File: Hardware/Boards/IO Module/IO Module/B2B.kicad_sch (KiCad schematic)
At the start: 0 parts

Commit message: Updated IO Module Schematics
Added Power, USB hub and USB-JTAG circuits
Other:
- company: (none) -> Drexel University
- title: (none) -> Board to Board Connectors
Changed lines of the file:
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@@
 	(generator "eeschema")
 	(generator_version "8.0")
-	(paper "A4")
+	(paper "A3")
+	(title_block
+		(title "Board to Board Connectors")
+		(date "2024-07-14")
+		(rev "1.0")
+		(company "Drexel University")
+		(comment 1 "Designed by John Hofmeyr")
+	)
 )

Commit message: Completed IO Module Schematics
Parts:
- added J2, J3: LSHM-130-XX.X-XXX-DV-A-S-K-XX, IO_Module:SAMTEC_LSHM-130-XX.X-XXX-DV-A-S-K-XX, symbol IO_Module:LSHM-130-XX.X-XXX-DV-A-S-K-XX
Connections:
- new net CAM_LED_EN: J3.52
- new net CAM_PWR_EN: J3.50
- new net FIFO_BE0: J2.34
- new net FIFO_BE1: J2.36
- new net FIFO_CLK: J3.01
- new net FIFO_D0: J3.03
- new net FIFO_D1: J3.05
- new net FIFO_D10: J3.06
- new net FIFO_D11: J3.08
- new net FIFO_D12: J3.10
- new net FIFO_D13: J3.12
- new net FIFO_D14: J3.14
- new net FIFO_D15: J3.16
- new net FIFO_D2: J3.07
- new net FIFO_D3: J3.09
- new net FIFO_D4: J3.11
- new net FIFO_D5: J3.13
- new net FIFO_D6: J3.15
- new net FIFO_D7: J3.17
- new net FIFO_D8: J3.02
- new net FIFO_D9: J3.04
- new net FPGA_I2C_SCL: J2.53
- new net FPGA_I2C_SDA: J2.55
- new net FT600_OE: J2.24
- new net FT600_RD: J2.26
- new net FT600_RST: J2.20
- new net FT600_RXE: J2.32
- new net FT600_TXE: J2.30
- new net FT600_WAKEUP: J2.22
- new net FT600_WR: J2.28
- new net GND: J2.05, J2.06, J2.07, J2.08, J2.14, J2.16, J2.18, J2.21, J2.27, J2.33, J2.38, J2.39, J2.45, J2.51, J2.S1 (SHIELD), J2.S2 (SHIELD__1), J3.18, J3.19, J3.36, J3.37, J3.42, J3.43, J3.48, J3.49, J3.54, J3.55, J3.56, J3.57, J3.58, J3.59, J3.60, J3.S1 (SHIELD), J3.S2 (SHIELD__1)
- new net HDMI_AUX_N: J2.47
- new net HDMI_AUX_P: J2.49
- new net HDMI_CEC: J2.60
- new net HDMI_CEC_EN: J2.52
- new net HDMI_CLK_N: J2.41
- new net HDMI_CLK_P: J2.43
- new net HDMI_D0_N: J2.35
- new net HDMI_D0_P: J2.37
- new net HDMI_D1_N: J2.29
- new net HDMI_D1_P: J2.31
- new net HDMI_D2_N: J2.23
- new net HDMI_D2_P: J2.25
- new net HDMI_EQ_SEL: J2.46
- new net HDMI_HPD_SRC: J2.58
- new net HDMI_I2C_EN: J2.42
- new net HDMI_OE: J2.56
- new net HDMI_PRE_SEL: J2.44
- new net HDMI_SCL_SRC: J2.57
- new net HDMI_SDA_SRC: J2.59
- new net HDMI_SEL: J2.48
- new net HDMI_SLEW_CTL: J2.54
- new net HDMI_SWAP: J2.40
- new net HDMI_TX_TERM_CTL: J2.50
- new net JTAG_TCK: J2.11
- new net JTAG_TDI: J2.15
- new net JTAG_TDO: J2.13
- new net JTAG_TMS: J2.09
- new net MBUS_D0: J3.21
- new net MBUS_D1: J3.23
- new net MBUS_D10: J3.24
- new net MBUS_D11: J3.26
- new net MBUS_D12: J3.28
- new net MBUS_D13: J3.30
- new net MBUS_D14: J3.32
- new net MBUS_D15: J3.34
- new net MBUS_D2: J3.25
- new net MBUS_D3: J3.27
- new net MBUS_D4: J3.29
- new net MBUS_D5: J3.31
- new net MBUS_D6: J3.33
- new net MBUS_D7: J3.35
- new net MBUS_D8: J3.20
- new net MBUS_D9: J3.22
- new net MIPI_CLK_N: J3.53
- new net MIPI_CLK_P: J3.51
- new net MIPI_D0_N: J3.41
- new net MIPI_D0_P: J3.39
- new net MIPI_D1_N: J3.47
- new net MIPI_D1_P: J3.45
- new net MIPI_D2_N: J3.40
- new net MIPI_D2_P: J3.38
- new net MIPI_D3_N: J3.46
- new net MIPI_D3_P: J3.44
- new net PP_VUSB: J2.01, J2.02, J2.03, J2.04
- new net UART_RX: J2.17
- new net UART_TX: J2.19
- new net USB_SYSMON_D_N: J2.12
- new net USB_SYSMON_D_P: J2.10

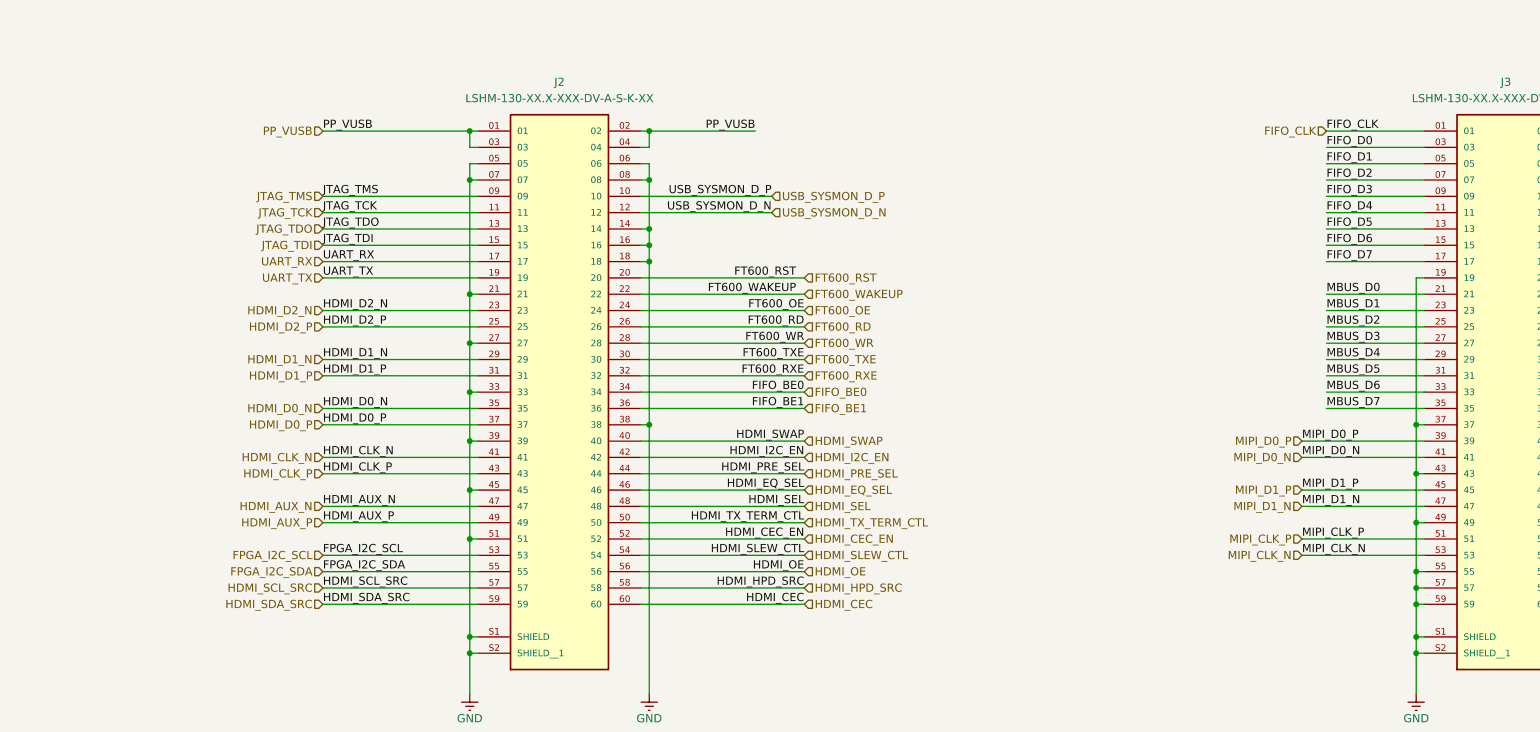
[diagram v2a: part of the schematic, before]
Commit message: Updated SCH with notes & annotations
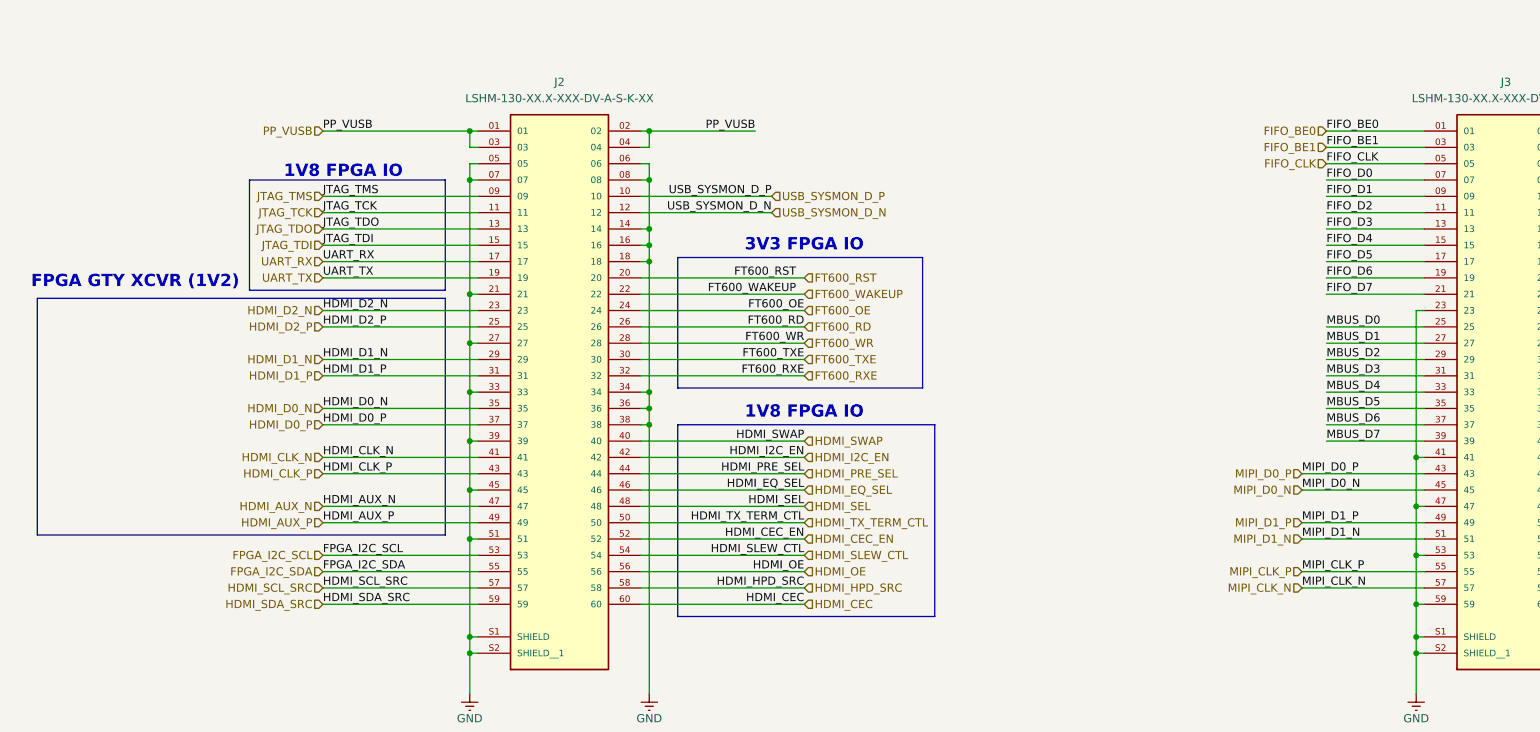
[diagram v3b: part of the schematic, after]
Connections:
- net FIFO_BE0: now also J3.01; no longer J2.34
- net FIFO_BE1: now also J3.03; no longer J2.36
- net FIFO_CLK: now also J3.05; no longer J3.01
- net FIFO_D0: now also J3.07; no longer J3.03
- net FIFO_D1: now also J3.09; no longer J3.05
- net FIFO_D2: now also J3.11; no longer J3.07
- net FIFO_D3: now also J3.13; no longer J3.09
- net FIFO_D4: now also J3.15; no longer J3.11
- net FIFO_D5: now also J3.17; no longer J3.13
- net FIFO_D6: now also J3.19; no longer J3.15
- net FIFO_D7: now also J3.21; no longer J3.17
- net GND: now also J2.34, J2.36, J3.23, J3.41, J3.47, J3.53; no longer J3.19, J3.37, J3.43, J3.49, J3.55, J3.57
- net MBUS_D0: now also J3.25; no longer J3.21
- net MBUS_D1: now also J3.27; no longer J3.23
- net MBUS_D2: now also J3.29; no longer J3.25
- net MBUS_D3: now also J3.31; no longer J3.27
- net MBUS_D4: now also J3.33; no longer J3.29
- net MBUS_D5: now also J3.35; no longer J3.31
- net MBUS_D6: now also J3.37; no longer J3.33
- net MBUS_D7: now also J3.39; no longer J3.35
- net MIPI_CLK_N: now also J3.57; no longer J3.53
- net MIPI_CLK_P: now also J3.55; no longer J3.51
- net MIPI_D0_N: now also J3.45; no longer J3.41
- net MIPI_D0_P: now also J3.43; no longer J3.39
- net MIPI_D1_N: now also J3.51; no longer J3.47
- net MIPI_D1_P: now also J3.49; no longer J3.45
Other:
- note added: "1V8 FPGA IO"
- note added: "3V3 FPGA IO"
- note added: "FPGA GTY XCVR (1V2)"

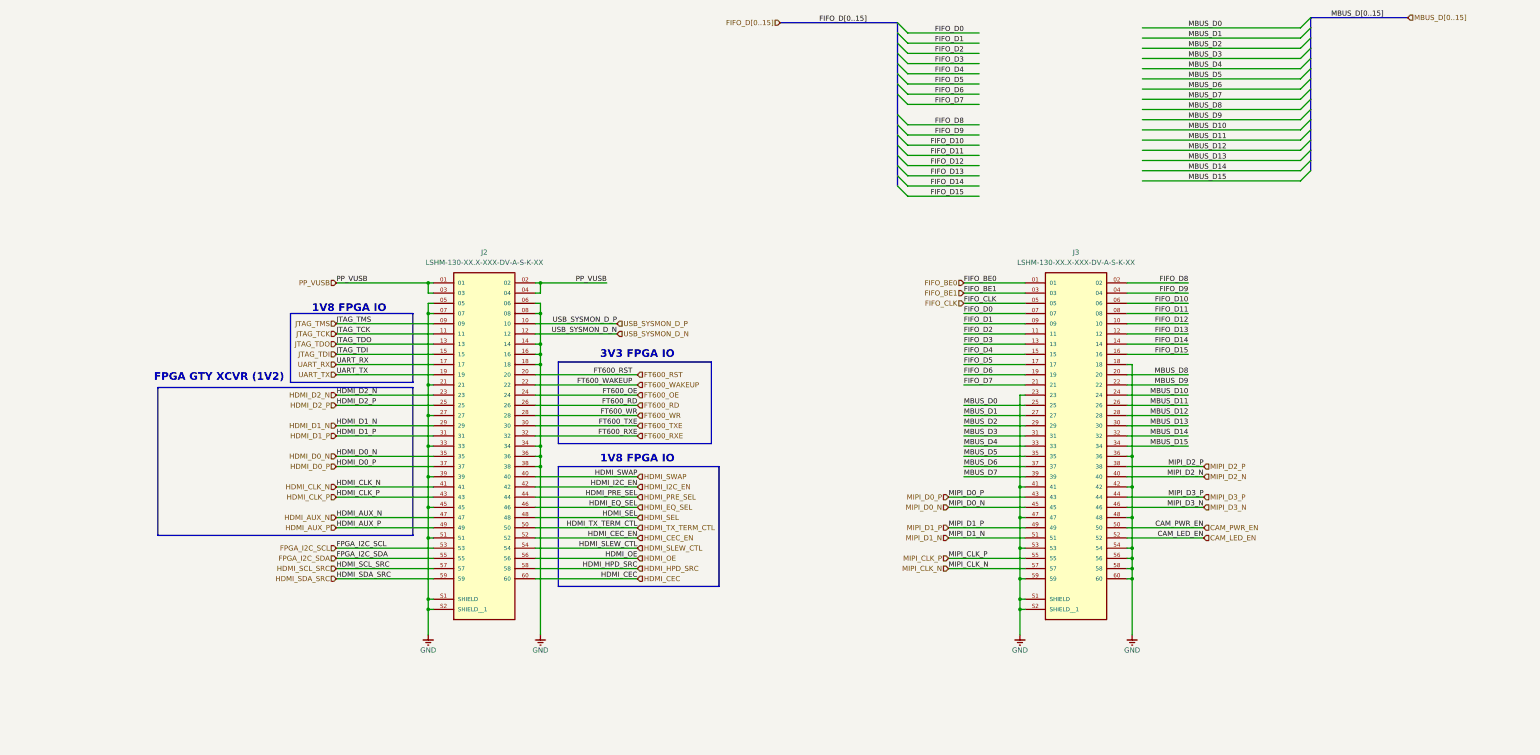
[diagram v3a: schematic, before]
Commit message: Updated PCB routing for IO Module
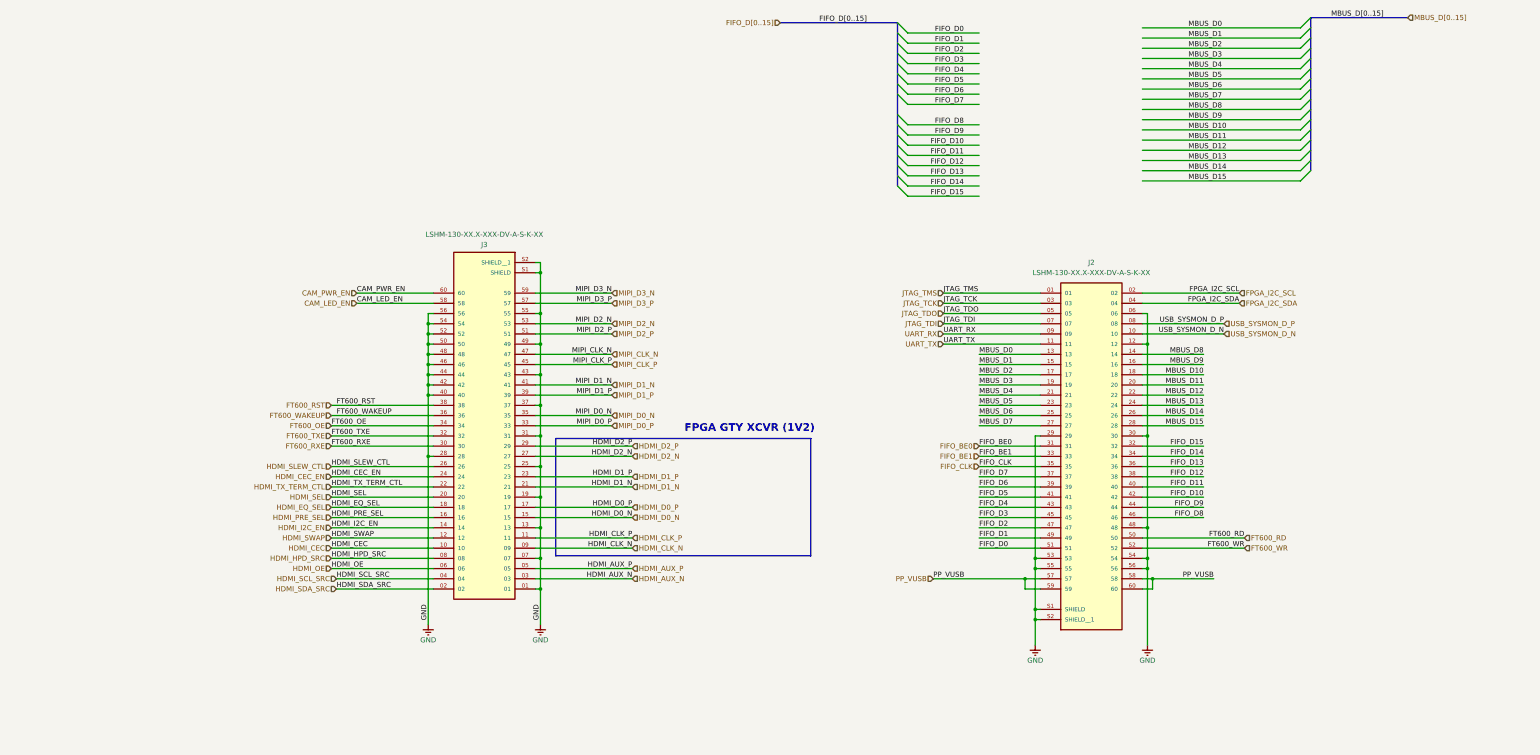
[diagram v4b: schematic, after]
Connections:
- net CAM_LED_EN: now also J3.58; no longer J3.52
- net CAM_PWR_EN: now also J3.60; no longer J3.50
- net FIFO_BE0: now also J2.31; no longer J3.01
- net FIFO_BE1: now also J2.33; no longer J3.03
- net FIFO_CLK: now also J2.35; no longer J3.05
- net FIFO_D0: now also J2.51; no longer J3.07
- net FIFO_D1: now also J2.49; no longer J3.09
- net FIFO_D10: now also J2.42; no longer J3.06
- net FIFO_D11: now also J2.40; no longer J3.08
- net FIFO_D12: now also J2.38; no longer J3.10
- net FIFO_D13: now also J2.36; no longer J3.12
- net FIFO_D14: now also J2.34; no longer J3.14
- net FIFO_D15: now also J2.32; no longer J3.16
- net FIFO_D2: now also J2.47; no longer J3.11
- net FIFO_D3: now also J2.45; no longer J3.13
- net FIFO_D4: now also J2.43; no longer J3.15
- net FIFO_D5: now also J2.41; no longer J3.17
- net FIFO_D6: now also J2.39; no longer J3.19
- net FIFO_D7: now also J2.37; no longer J3.21
- net FIFO_D8: now also J2.46; no longer J3.02
- net FIFO_D9: now also J2.44; no longer J3.04
- net FPGA_I2C_SCL: now also J2.02; no longer J2.53
- net FPGA_I2C_SDA: now also J2.04; no longer J2.55
- net FT600_OE: now also J3.34; no longer J2.24
- net FT600_RD: now also J2.50; no longer J2.26
- net FT600_RST: now also J3.38; no longer J2.20
- net FT600_RXE: now also J3.30; no longer J2.32
- net FT600_TXE: now also J3.32; no longer J2.30
- net FT600_WAKEUP: now also J3.36; no longer J2.22
- net FT600_WR: now also J2.52; no longer J2.28
- net GND: now also J2.12, J2.29, J2.30, J2.48, J2.53, J2.54, J2.55, J2.56, J3.01, J3.07, J3.13, J3.19, J3.25, J3.28, J3.31, J3.37, J3.40, J3.43, J3.44, J3.46, J3.49, J3.50, J3.52, J3.55; no longer J2.05, J2.07, J2.08, J2.14, J2.16, J2.18, J2.21, J2.27, J2.33, J2.34, J2.36, J2.38, J2.39, J2.45, J2.51, J3.18, J3.23, J3.36, J3.41, J3.47, J3.53, J3.58, J3.59, J3.60
- net HDMI_AUX_N: now also J3.03; no longer J2.47
- net HDMI_AUX_P: now also J3.05; no longer J2.49
- net HDMI_CEC: now also J3.10; no longer J2.60
- net HDMI_CEC_EN: now also J3.24; no longer J2.52
- net HDMI_CLK_N: now also J3.09; no longer J2.41
- net HDMI_CLK_P: now also J3.11; no longer J2.43
- net HDMI_D0_N: now also J3.15; no longer J2.35
- net HDMI_D0_P: now also J3.17; no longer J2.37
- net HDMI_D1_N: now also J3.21; no longer J2.29
- net HDMI_D1_P: now also J3.23; no longer J2.31
- net HDMI_D2_N: now also J3.27; no longer J2.23
- net HDMI_D2_P: now also J3.29; no longer J2.25
- net HDMI_EQ_SEL: now also J3.18; no longer J2.46
- net HDMI_HPD_SRC: now also J3.08; no longer J2.58
- net HDMI_I2C_EN: now also J3.14; no longer J2.42
- net HDMI_OE: now also J3.06; no longer J2.56
- net HDMI_PRE_SEL: now also J3.16; no longer J2.44
- net HDMI_SCL_SRC: now also J3.04; no longer J2.57
- net HDMI_SDA_SRC: now also J3.02; no longer J2.59
- net HDMI_SEL: now also J3.20; no longer J2.48
- net HDMI_SLEW_CTL: now also J3.26; no longer J2.54
- net HDMI_SWAP: now also J3.12; no longer J2.40
- net HDMI_TX_TERM_CTL: now also J3.22; no longer J2.50
- net JTAG_TCK: now also J2.03; no longer J2.11
- net JTAG_TDI: now also J2.07; no longer J2.15
- net JTAG_TDO: now also J2.05; no longer J2.13
- net JTAG_TMS: now also J2.01; no longer J2.09
- net MBUS_D0: now also J2.13; no longer J3.25
- net MBUS_D1: now also J2.15; no longer J3.27
- net MBUS_D10: now also J2.18; no longer J3.24
- net MBUS_D11: now also J2.20; no longer J3.26
- net MBUS_D12: now also J2.22; no longer J3.28
- net MBUS_D13: now also J2.24; no longer J3.30
- net MBUS_D14: now also J2.26; no longer J3.32
- net MBUS_D15: now also J2.28; no longer J3.34
- net MBUS_D2: now also J2.17; no longer J3.29
- net MBUS_D3: now also J2.19; no longer J3.31
- net MBUS_D4: now also J2.21; no longer J3.33
- net MBUS_D5: now also J2.23; no longer J3.35
- net MBUS_D6: now also J2.25; no longer J3.37
- net MBUS_D7: now also J2.27; no longer J3.39
- net MBUS_D8: now also J2.14; no longer J3.20
- net MBUS_D9: now also J2.16; no longer J3.22
- net MIPI_CLK_N: now also J3.47; no longer J3.57
- net MIPI_CLK_P: now also J3.45; no longer J3.55
- net MIPI_D0_N: now also J3.35; no longer J3.45
- net MIPI_D0_P: now also J3.33; no longer J3.43
- net MIPI_D1_N: now also J3.41; no longer J3.51
- net MIPI_D1_P: now also J3.39; no longer J3.49
- net MIPI_D2_N: now also J3.53; no longer J3.40
- net MIPI_D2_P: now also J3.51; no longer J3.38
- net MIPI_D3_N: now also J3.59; no longer J3.46
- net MIPI_D3_P: now also J3.57; no longer J3.44
- net PP_VUSB: now also J2.57, J2.58, J2.59, J2.60; no longer J2.01, J2.02, J2.03, J2.04
- net UART_RX: now also J2.09; no longer J2.17
- net UART_TX: now also J2.11; no longer J2.19
- net USB_SYSMON_D_N: now also J2.10; no longer J2.12
- net USB_SYSMON_D_P: now also J2.08; no longer J2.10
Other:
- note removed: "1V8 FPGA IO"
- note removed: "3V3 FPGA IO"
- moved on the sheet: J2

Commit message: Completed IO Module PCB Layout
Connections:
- net FIFO_BE0: now also J2.33; no longer J2.31
- net FIFO_BE1: now also J2.31; no longer J2.33
- net FT600_RST: now also J3.36; no longer J3.38
- net FT600_RXE: now also J3.32; no longer J3.30
- net FT600_TXE: now also J3.30; no longer J3.32
- net FT600_WAKEUP: now also J3.38; no longer J3.36
- net HDMI_CEC: now also J3.02; no longer J3.10
- net HDMI_HPD_SRC: now also J3.10; no longer J3.08
- net HDMI_I2C_EN: now also J3.12; no longer J3.14
- net HDMI_OE: now also J3.04; no longer J3.06
- net HDMI_SCL_SRC: now also J3.06; no longer J3.04
- net HDMI_SDA_SRC: now also J3.08; no longer J3.02
- net HDMI_SWAP: now also J3.14; no longer J3.12
- net JTAG_TCK: now also J2.01; no longer J2.03
- net JTAG_TDI: now also J2.03; no longer J2.07
- net JTAG_TMS: now also J2.07; no longer J2.01

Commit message: Cleaned up routing for IO module
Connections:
- net MBUS_D15 is gone; now on net GND: J2.28
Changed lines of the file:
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@@
 	)
 	(junction
+		(at 297.18 130.81)
+		(diameter 0)
+		(color 0 0 0 0)
+	)
+	(junction
 		(at 118.11 118.11)
 		(diameter 0)
@@
 	)
 	(bus_entry
-		(at 335.28 69.85)
-		(size 2.54 -2.54)
-		(stroke
-			(width 0)
-			(type default)
-		)
-	)
-	(bus_entry
 		(at 335.28 52.07)
 		(size 2.54 -2.54)
@@
 	(wire
 		(pts
-			(xy 295.91 130.81) (xy 311.15 130.81)
-		)
-		(stroke
-			(width 0)
-			(type default)
-		)
-	)
-	(wire
-		(pts
 			(xy 146.05 92.71) (xy 146.05 90.17)
 		)
@@
 	(wire
 		(pts
-			(xy 295.91 69.85) (xy 335.28 69.85)
+			(xy 93.98 168.91) (xy 119.38 168.91)
 		)
 		(stroke
@@
 	(wire
 		(pts
-			(xy 93.98 168.91) (xy 119.38 168.91)
+			(xy 295.91 156.21) (xy 297.18 156.21)
 		)
 		(stroke
@@
 		)
 	)
-	(wire
+	(bus
 		(pts
-			(xy 295.91 156.21) (xy 297.18 156.21)
+			(xy 337.82 54.61) (xy 337.82 52.07)
 		)
 		(stroke
@@
 		)
 	)
-	(bus
+	(wire
 		(pts
-			(xy 337.82 54.61) (xy 337.82 52.07)
+			(xy 255.27 63.5) (xy 237.49 63.5)
 		)
 		(stroke
@@
 	(wire
 		(pts
-			(xy 255.27 63.5) (xy 237.49 63.5)
+			(xy 297.18 130.81) (xy 297.18 133.35)
 		)
 		(stroke
@@
 	(wire
 		(pts
-			(xy 295.91 59.69) (xy 335.28 59.69)
+			(xy 295.91 130.81) (xy 297.18 130.81)
 		)
 		(stroke
@@
 	(wire
 		(pts
-			(xy 119.38 151.13) (xy 93.98 151.13)
+			(xy 295.91 59.69) (xy 335.28 59.69)
 		)
 		(stroke
@@
 	(wire
 		(pts
-			(xy 146.05 180.34) (xy 146.05 171.45)
+			(xy 119.38 151.13) (xy 93.98 151.13)
 		)
 		(stroke
@@
 	(wire
 		(pts
-			(xy 144.78 125.73) (xy 146.05 125.73)
+			(xy 146.05 180.34) (xy 146.05 171.45)
 		)
 		(stroke
@@
 		)
 	)
-	(bus
+	(wire
 		(pts
-			(xy 337.82 67.31) (xy 337.82 64.77)
+			(xy 144.78 125.73) (xy 146.05 125.73)
 		)
 		(stroke
@@
 	(wire
 		(pts
-			(xy 297.18 110.49) (xy 297.18 133.35)
+			(xy 297.18 110.49) (xy 297.18 130.81)
 		)
 		(stroke
@@
 		)
 	)
-	(label "MBUS_D15"
-		(at 307.34 69.85 0)
-		(fields_autoplaced yes)
-		(effects
-			(font
-				(size 1.27 1.27)
-			)
-			(justify left bottom)
-		)
-	)
 	(label "FIFO_D10"
 		(at 251.46 60.96 180)
@@
 		)
 	)
-	(label "MBUS_D15"
-		(at 311.15 130.81 180)
-		(fields_autoplaced yes)
-		(effects
-			(font
-				(size 1.27 1.27)
-			)
-			(justify right bottom)
-		)
-	)
 	(label "HDMI_SDA_SRC"
 		(at 93.98 163.83 0)
@@
 		)
 	)
-	(label "MBUS_D[0..15]"
+	(label "MBUS_D[0..14]"
 		(at 342.9 29.21 0)
 		(fields_autoplaced yes)
@@
 		)
 	)
-	(hierarchical_label "MBUS_D[0..15]"
+	(hierarchical_label "MBUS_D[0..14]"
 		(shape input)
 		(at 361.95 29.21 0)
